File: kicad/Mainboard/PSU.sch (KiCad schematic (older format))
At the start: 20 parts, among them J5 BATT, J6 POT_PWR_SW, U3 LD1117S50TR_SOT223, U4 LD1117S33TR_SOT223

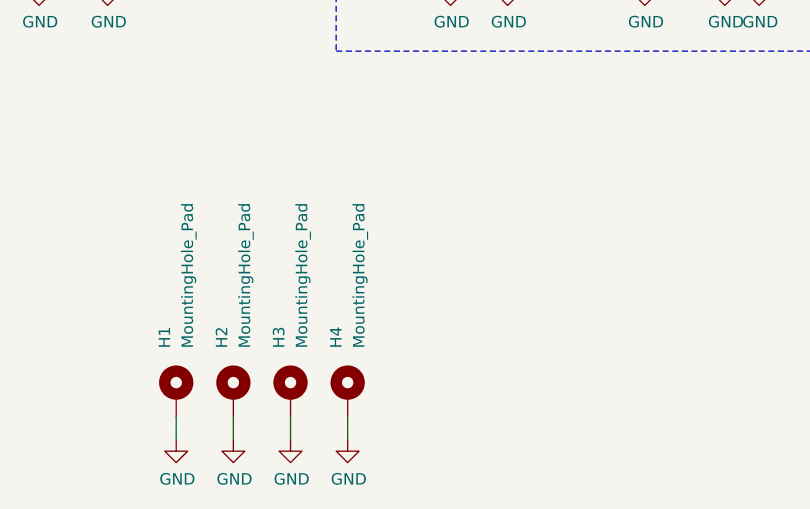
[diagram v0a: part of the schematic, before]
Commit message: RF power amp, and RF chipset on pcb
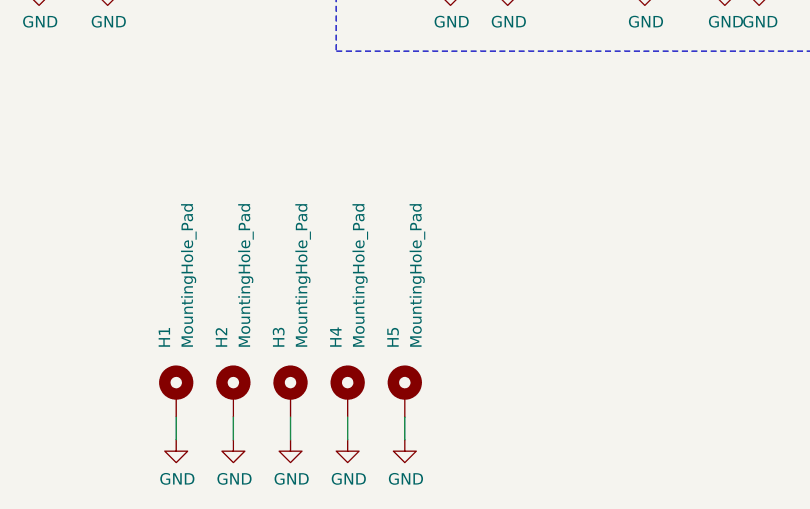
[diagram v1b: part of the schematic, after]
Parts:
- added H5: MountingHole_Pad, MountingHole:MountingHole_2.2mm_M2_ISO14580_Pad, symbol Mainboard-rescue:MountingHole_Pad-mechanical
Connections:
- net GND: now also H5.1
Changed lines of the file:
@@
 Wire Wire Line
 	5900 4350 5900 4150
+$Comp
+L Mainboard-rescue:MountingHole_Pad-mechanical H5
+U 1 1 5E5173B7
+P 4500 6150
+F 0 "H5" V 4450 6350 50  0000 L CNN
+F 1 "MountingHole_Pad" V 4550 6350 50  0000 L CNN
+F 2 "MountingHole:MountingHole_2.2mm_M2_ISO14580_Pad" H 4500 6150 50  0001 C CNN
+F 3 "~" H 4500 6150 50  0001 C CNN
+	1    4500 6150
+	1    0    0    -1
+$EndComp
+$Comp
+L power:GND #PWR0206
+U 1 1 5E5178E2
+P 4500 6350
+F 0 "#PWR0206" H 4500 6100 50  0001 C CNN
+F 1 "GND" H 4505 6177 50  0000 C CNN
+F 2 "" H 4500 6350 50  0001 C CNN
+F 3 "" H 4500 6350 50  0001 C CNN
+	1    4500 6350
+	1    0    0    -1
+$EndComp
+Wire Wire Line
+	4500 6250 4500 6350
 $EndSCHEMATC

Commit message: changed BATT cap
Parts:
- C8: footprint Capacitor_Tantalum_SMD:CP_EIA-3216-18_Kemet-A -> Capacitor_THT:CP_Radial_D4.0mm_P2.00mm
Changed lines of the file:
@@
 F 0 "C8" V 4425 3550 50  0000 C CNN
 F 1 "22u/TA" V 4516 3550 50  0000 C CNN
-F 2 "Capacitor_Tantalum_SMD:CP_EIA-3216-18_Kemet-A" H 4650 3550 50  0001 C CNN
+F 2 "Capacitor_THT:CP_Radial_D4.0mm_P2.00mm" H 4650 3550 50  0001 C CNN
 F 3 "~" H 4650 3550 50  0001 C CNN
 F 4 "TAJA226K006RNJV" H 4650 3550 50  0001 C CNN "Partno"

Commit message: some small changes
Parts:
- removed H5: MountingHole_Pad, MountingHole:MountingHole_2.2mm_M2_ISO14580_Pad, symbol Mainboard-rescue:MountingHole_Pad-mechanical
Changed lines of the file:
@@
-$EndComp
-$Comp
-L Mainboard-rescue:MountingHole_Pad-mechanical H4
-U 1 1 5DEEC94F
-P 4250 6150
-F 0 "H4" V 4200 6350 50  0000 L CNN
-F 1 "MountingHole_Pad" V 4300 6350 50  0000 L CNN
-F 2 "MountingHole:MountingHole_2.2mm_M2_ISO14580_Pad" H 4250 6150 50  0001 C CNN
-F 3 "~" H 4250 6150 50  0001 C CNN
-	1    4250 6150
-	1    0    0    -1
 $EndComp
 $Comp
@@
 	1    0    0    -1
 $EndComp
-$Comp
-L power:GND #PWR036
-U 1 1 5DEED62E
-P 4250 6350
-F 0 "#PWR036" H 4250 6100 50  0001 C CNN
-F 1 "GND" H 4255 6177 50  0000 C CNN
-F 2 "" H 4250 6350 50  0001 C CNN
-F 3 "" H 4250 6350 50  0001 C CNN
-	1    4250 6350
-	1    0    0    -1
-$EndComp
-Wire Wire Line
-	4250 6250 4250 6350
 Wire Wire Line
 	4000 6250 4000 6350
@@
 Wire Wire Line
 	5900 4350 5900 4150
-$Comp
-L Mainboard-rescue:MountingHole_Pad-mechanical H5
-U 1 1 5E5173B7
-P 4500 6150
-F 0 "H5" V 4450 6350 50  0000 L CNN
-F 1 "MountingHole_Pad" V 4550 6350 50  0000 L CNN
-F 2 "MountingHole:MountingHole_2.2mm_M2_ISO14580_Pad" H 4500 6150 50  0001 C CNN
-F 3 "~" H 4500 6150 50  0001 C CNN
-	1    4500 6150
-	1    0    0    -1
-$EndComp
-$Comp
-L power:GND #PWR0206
-U 1 1 5E5178E2
-P 4500 6350
-F 0 "#PWR0206" H 4500 6100 50  0001 C CNN
-F 1 "GND" H 4505 6177 50  0000 C CNN
-F 2 "" H 4500 6350 50  0001 C CNN
-F 3 "" H 4500 6350 50  0001 C CNN
-	1    4500 6350
-	1    0    0    -1
-$EndComp
-Wire Wire Line
-	4500 6250 4500 6350
+Wire Wire Line
+	4250 6250 4250 6350
+$Comp
+L power:GND #PWR036
+U 1 1 5DEED62E
+P 4250 6350
+F 0 "#PWR036" H 4250 6100 50  0001 C CNN
+F 1 "GND" H 4255 6177 50  0000 C CNN
+F 2 "" H 4250 6350 50  0001 C CNN
+F 3 "" H 4250 6350 50  0001 C CNN
+	1    4250 6350
+	1    0    0    -1
+$EndComp
+$Comp
+L Mainboard-rescue:MountingHole_Pad-mechanical H4
+U 1 1 5DEEC94F
+P 4250 6150
+F 0 "H4" V 4200 6350 50  0000 L CNN
+F 1 "MountingHole_Pad" V 4300 6350 50  0000 L CNN
+F 2 "MountingHole:MountingHole_2.2mm_M2_ISO14580_Pad" H 4250 6150 50  0001 C CNN
+F 3 "~" H 4250 6150 50  0001 C CNN
+	1    4250 6150
+	1    0    0    -1
+$EndComp
 $EndSCHEMATC

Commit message: added few values in BOM
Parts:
- C10, C9: Tolerance (none) -> 10; Voltage (none) -> 25
- C11, C13, C15, C17, C98: Tolerance (none) -> 10; Voltage (none) -> 6.3
- C8: value 22u/TA -> 22u; Tolerance (none) -> 10; Voltage (none) -> 25
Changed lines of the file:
@@
 P 4650 3550
 F 0 "C8" V 4425 3550 50  0000 C CNN
-F 1 "22u/TA" V 4516 3550 50  0000 C CNN
+F 1 "22u" V 4516 3550 50  0000 C CNN
 F 2 "Capacitor_THT:CP_Radial_D4.0mm_P2.00mm" H 4650 3550 50  0001 C CNN
 F 3 "~" H 4650 3550 50  0001 C CNN
 F 4 "TAJA226K006RNJV" H 4650 3550 50  0001 C CNN "Partno"
+F 5 "10" H 4650 3550 50  0001 C CNN "Tolerance"
+F 6 "25" H 4650 3550 50  0001 C CNN "Voltage"
 	1    4650 3550
 	0    1    1    0
@@
 F 2 "Capacitor_SMD:C_0603_1608Metric" H 4700 4150 50  0001 C CNN
 F 3 "~" H 4700 4150 50  0001 C CNN
+F 4 "10" H 4700 4150 50  0001 C CNN "Tolerance"
+F 5 "25" H 4700 4150 50  0001 C CNN "Voltage"
 	1    4700 4150
 	1    0    0    1
@@
 F 3 "~" H 7950 3850 50  0001 C CNN
 F 4 "TAJA226K006RNJV" H 7950 3850 50  0001 C CNN "Partno"
+F 5 "10" H 7950 3850 50  0001 C CNN "Tolerance"
+F 6 "6.3" H 7950 3850 50  0001 C CNN "Voltage"
 	1    7950 3850
 	1    0    0    -1
@@
 F 3 "~" H 8450 3850 50  0001 C CNN
 F 4 "TAJA226K006RNJV" H 8450 3850 50  0001 C CNN "Partno"
+F 5 "10" H 8450 3850 50  0001 C CNN "Tolerance"
+F 6 "6.3" H 8450 3850 50  0001 C CNN "Voltage"
 	1    8450 3850
 	1    0    0    -1
@@
 F 3 "~" H 8950 3850 50  0001 C CNN
 F 4 "TAJA226K006RNJV" H 8950 3850 50  0001 C CNN "Partno"
+F 5 "10" H 8950 3850 50  0001 C CNN "Tolerance"
+F 6 "6.3" H 8950 3850 50  0001 C CNN "Voltage"
 	1    8950 3850
 	1    0    0    -1
@@
 F 3 "~" H 9450 3850 50  0001 C CNN
 F 4 "TAJA226K006RNJV" H 9450 3850 50  0001 C CNN "Partno"
+F 5 "10" H 9450 3850 50  0001 C CNN "Tolerance"
+F 6 "6.3" H 9450 3850 50  0001 C CNN "Voltage"
 	1    9450 3850
 	1    0    0    -1
@@
 F 2 "Capacitor_SMD:C_0603_1608Metric" H 6050 4050 50  0001 C CNN
 F 3 "~" H 6050 4050 50  0001 C CNN
+F 4 "25" H 6050 4050 50  0001 C CNN "Voltage"
+F 5 "10" H 6050 4050 50  0001 C CNN "Tolerance"
 	1    6050 4050
 	1    0    0    -1
@@
 F 3 "~" H 5900 4050 50  0001 C CNN
 F 4 "TAJA226K006RNJV" H 5900 4050 50  0001 C CNN "Partno"
+F 5 "10" H 5900 4050 50  0001 C CNN "Tolerance"
+F 6 "6.3" H 5900 4050 50  0001 C CNN "Voltage"
 	1    5900 4050
 	1    0    0    -1

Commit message: Mainboard: List of components -> Added TempCoef types, voltage values and tolerance for capaciors; added power values and tolerance for resistors
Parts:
- C10, C9: TempCoef (none) -> X7R; Voltage 25 -> 50
- C11, C13, C15, C17, C98: TempCoef (none) -> TANTAL; Voltage 6.3 -> 10
- C8: TempCoef (none) -> ELEC
- R6, R7: Power (none) -> 0.125; Tolerance (none) -> 5
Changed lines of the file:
@@
 F 5 "10" H 4650 3550 50  0001 C CNN "Tolerance"
 F 6 "25" H 4650 3550 50  0001 C CNN "Voltage"
+F 7 "ELEC" H 4650 3550 50  0001 C CNN "TempCoef"
 	1    4650 3550
 	0    1    1    0
@@
 F 2 "Resistor_SMD:R_0603_1608Metric" H 4950 3750 50  0001 C CNN
 F 3 "~" H 4950 3750 50  0001 C CNN
+F 4 "0.125" H 4950 3750 50  0001 C CNN "Power"
+F 5 "5" H 4950 3750 50  0001 C CNN "Tolerance"
 	1    4950 3750
 	1    0    0    -1
@@
 F 2 "Resistor_SMD:R_0603_1608Metric" H 4950 4150 50  0001 C CNN
 F 3 "~" H 4950 4150 50  0001 C CNN
+F 4 "0.125" H 4950 4150 50  0001 C CNN "Power"
+F 5 "5" H 4950 4150 50  0001 C CNN "Tolerance"
 	1    4950 4150
 	1    0    0    -1
@@
 F 3 "~" H 4700 4150 50  0001 C CNN
 F 4 "10" H 4700 4150 50  0001 C CNN "Tolerance"
-F 5 "25" H 4700 4150 50  0001 C CNN "Voltage"
+F 5 "50" H 4700 4150 50  0001 C CNN "Voltage"
+F 6 "X7R" H 4700 4150 50  0001 C CNN "TempCoef"
 	1    4700 4150
 	1    0    0    1
@@
 F 4 "TAJA226K006RNJV" H 7950 3850 50  0001 C CNN "Partno"
 F 5 "10" H 7950 3850 50  0001 C CNN "Tolerance"
-F 6 "6.3" H 7950 3850 50  0001 C CNN "Voltage"
+F 6 "10" H 7950 3850 50  0001 C CNN "Voltage"
+F 7 "TANTAL" H 7950 3850 50  0001 C CNN "TempCoef"
 	1    7950 3850
 	1    0    0    -1
@@
 F 4 "TAJA226K006RNJV" H 8450 3850 50  0001 C CNN "Partno"
 F 5 "10" H 8450 3850 50  0001 C CNN "Tolerance"
-F 6 "6.3" H 8450 3850 50  0001 C CNN "Voltage"
+F 6 "10" H 8450 3850 50  0001 C CNN "Voltage"
+F 7 "TANTAL" H 8450 3850 50  0001 C CNN "TempCoef"
 	1    8450 3850
 	1    0    0    -1
@@
 F 4 "TAJA226K006RNJV" H 8950 3850 50  0001 C CNN "Partno"
 F 5 "10" H 8950 3850 50  0001 C CNN "Tolerance"
-F 6 "6.3" H 8950 3850 50  0001 C CNN "Voltage"
+F 6 "10" H 8950 3850 50  0001 C CNN "Voltage"
+F 7 "TANTAL" H 8950 3850 50  0001 C CNN "TempCoef"
 	1    8950 3850
 	1    0    0    -1
@@
 F 4 "TAJA226K006RNJV" H 9450 3850 50  0001 C CNN "Partno"
 F 5 "10" H 9450 3850 50  0001 C CNN "Tolerance"
-F 6 "6.3" H 9450 3850 50  0001 C CNN "Voltage"
+F 6 "10" H 9450 3850 50  0001 C CNN "Voltage"
+F 7 "TANTAL" H 9450 3850 50  0001 C CNN "TempCoef"
 	1    9450 3850
 	1    0    0    -1
@@
 F 2 "Capacitor_SMD:C_0603_1608Metric" H 6050 4050 50  0001 C CNN
 F 3 "~" H 6050 4050 50  0001 C CNN
-F 4 "25" H 6050 4050 50  0001 C CNN "Voltage"
+F 4 "50" H 6050 4050 50  0001 C CNN "Voltage"
 F 5 "10" H 6050 4050 50  0001 C CNN "Tolerance"
+F 6 "X7R" H 6050 4050 50  0001 C CNN "TempCoef"
 	1    6050 4050
 	1    0    0    -1
@@
 F 4 "TAJA226K006RNJV" H 5900 4050 50  0001 C CNN "Partno"
 F 5 "10" H 5900 4050 50  0001 C CNN "Tolerance"
-F 6 "6.3" H 5900 4050 50  0001 C CNN "Voltage"
+F 6 "10" H 5900 4050 50  0001 C CNN "Voltage"
+F 7 "TANTAL" H 5900 4050 50  0001 C CNN "TempCoef"
 	1    5900 4050
 	1    0    0    -1
